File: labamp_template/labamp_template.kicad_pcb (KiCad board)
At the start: 2 copper layers, 55 x 26 mm, 13 parts, among them J1 Conn_02x06_Odd_Even, J2 Conn_02x06_Odd_Even, J3 Conn_01x03

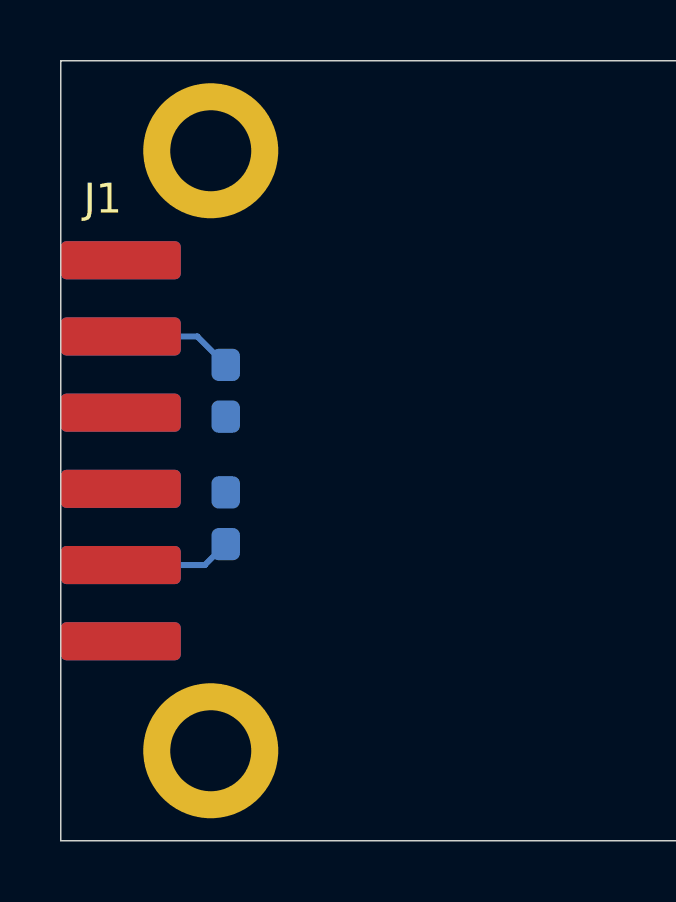
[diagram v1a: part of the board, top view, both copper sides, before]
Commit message: Moved mounting holes to avoid colision with header
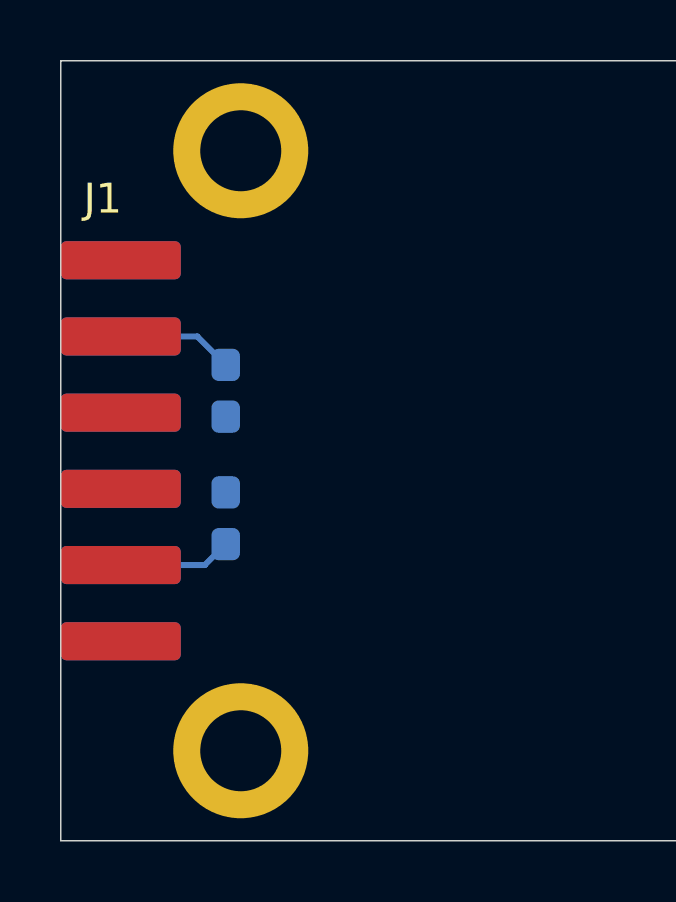
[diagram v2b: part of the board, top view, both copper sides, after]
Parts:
- moved H3 1.00 mm to (101.0, 100.0)
- moved H4 1.00 mm to (101.0, 80.0)
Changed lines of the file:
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@@
 			(psa4output no)
 			(plot_black_and_white yes)
-			(plotinvisibletext no)
 			(sketchpadsonfab no)
 			(plotpadnumbers no)
@@
 			(at 0 3.2 0)
 			(layer "F.Fab")
+			(hide yes)
 			(effects
 				(font
@@
 			(at 0 3.2 0)
 			(layer "F.Fab")
+			(hide yes)
 			(effects
 				(font
@@
 			(fill no)
 			(layer "F.CrtYd")
-		)
-		(fp_text user "${REFERENCE}"
-			(at 0 -3 0)
-			(layer "F.Fab")
-			(effects
-				(font
-					(size 1 1)
-					(thickness 0.15)
-				)
-			)
 		)
 		(pad "1" thru_hole circle
@@
 	(footprint "MountingHole:MountingHole_2.7mm_M2.5_ISO14580_Pad"
 		(layer "F.Cu")
-		(at 100 80)
+		(at 101 80)
 		(descr "Mounting Hole 2.7mm, M2.5, generated by kicad-footprint-generator mountinghole.py")
 		(tags "mountinghole M2.5 ISO14580")
@@
 	(footprint "MountingHole:MountingHole_2.7mm_M2.5_ISO14580_Pad"
 		(layer "F.Cu")
-		(at 100 100)
+		(at 101 100)
 		(descr "Mounting Hole 2.7mm, M2.5, generated by kicad-footprint-generator mountinghole.py")
 		(tags "mountinghole M2.5 ISO14580")
@@
 			(at 0 3.2 0)
 			(layer "F.Fab")
-			(effects
-				(font
+			(hide yes)
+			(effects
+				(font
